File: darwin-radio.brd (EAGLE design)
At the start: 110 x 73 mm, 50 parts, among them J1 S1911-46R, Q2 NDS8434, U1 ATWINC, U2 INA219, U6 MCP7384X

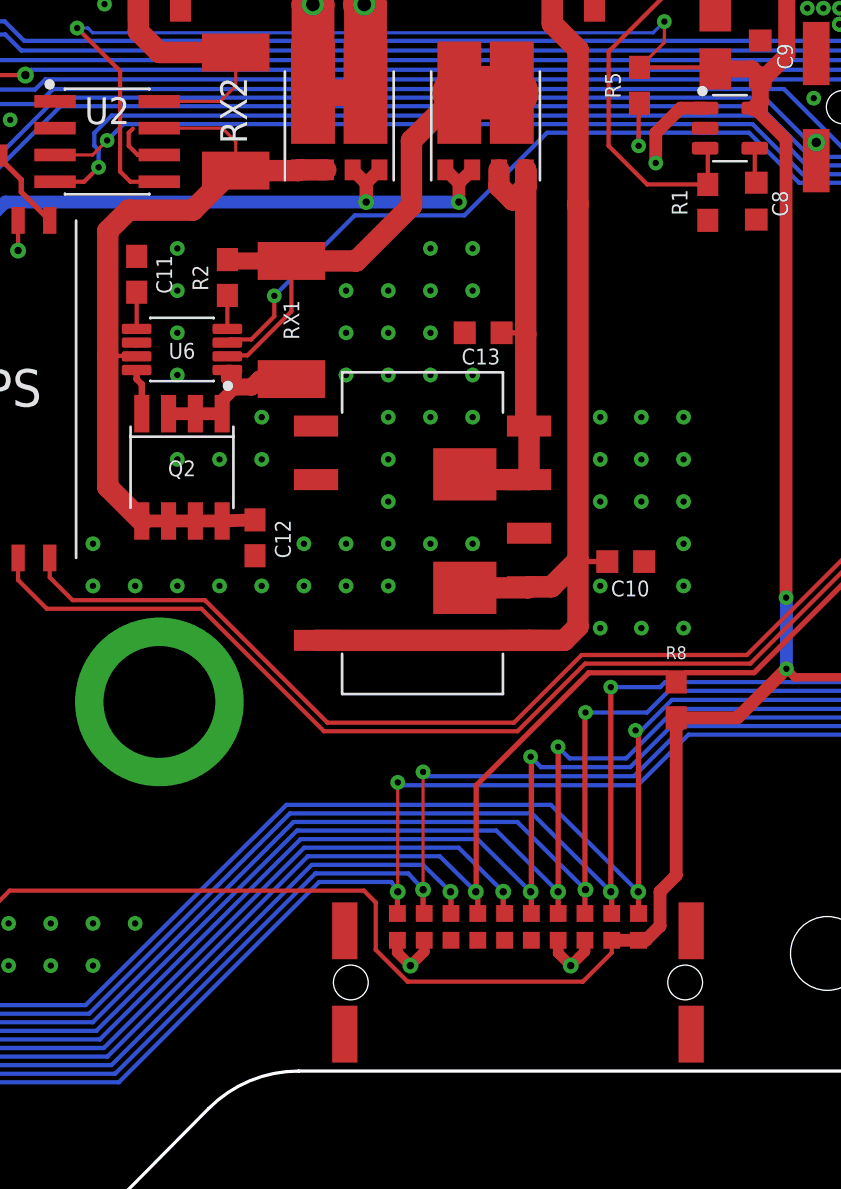
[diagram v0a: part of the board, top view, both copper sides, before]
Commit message: Toughened up connector footprints, cleaned up schematic, added schematic PDF.
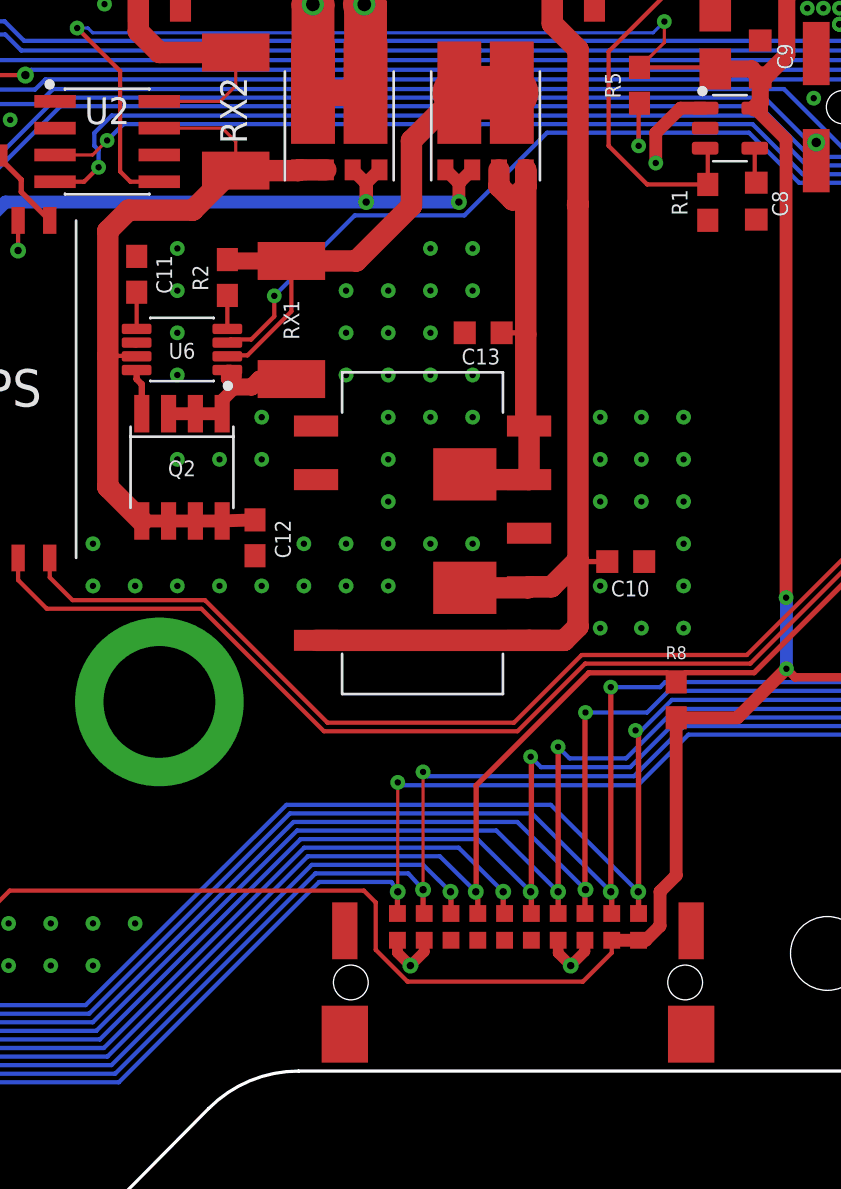
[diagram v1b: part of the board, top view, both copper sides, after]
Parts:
- RX1: value 100M -> 200m
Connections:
- net GND: now also BACKPLANE.PAD0, BACKPLANE.PAD1, BACKPLANE.PAD2, BACKPLANE.PAD3
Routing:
- net GND: track 111.1 -> 108.6 mm

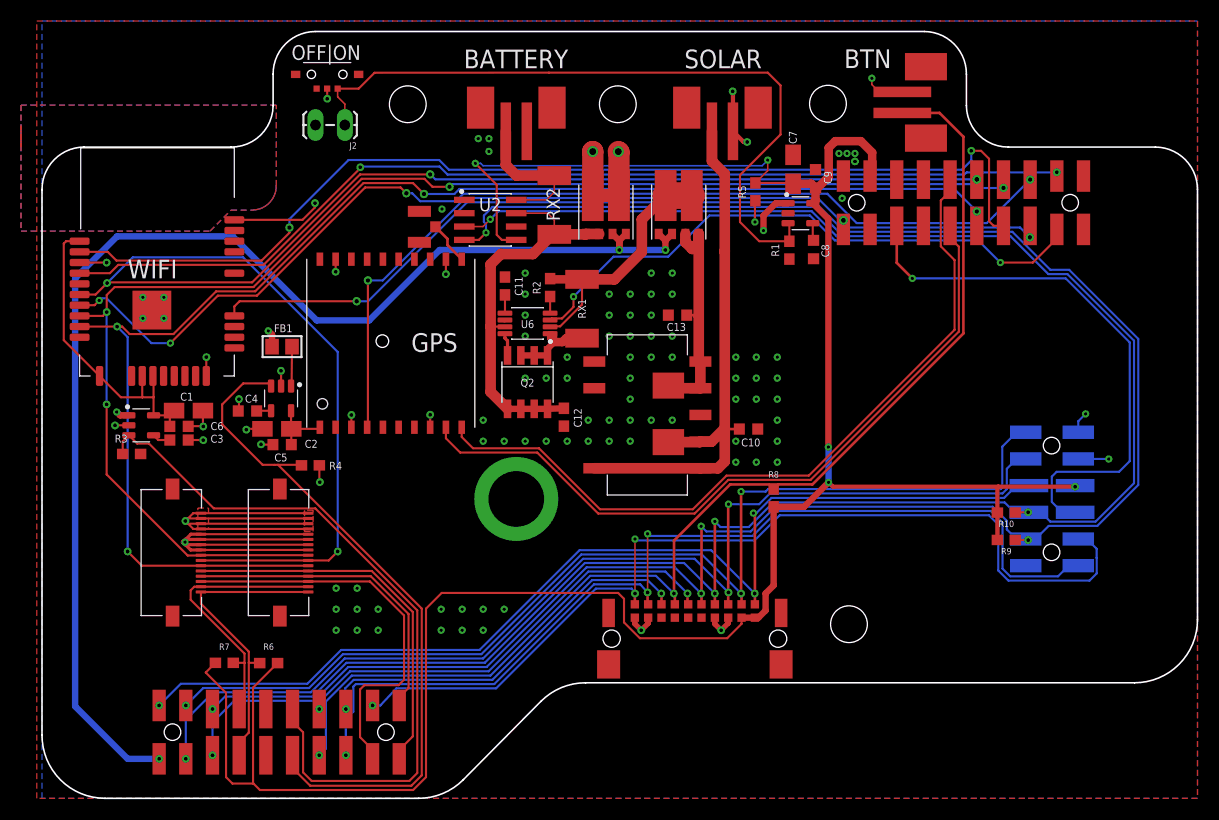
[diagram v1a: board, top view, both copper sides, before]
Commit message: Transitioned from 4 to 2 layers. Added solar power monitor. Changed GPS to L80-M39.
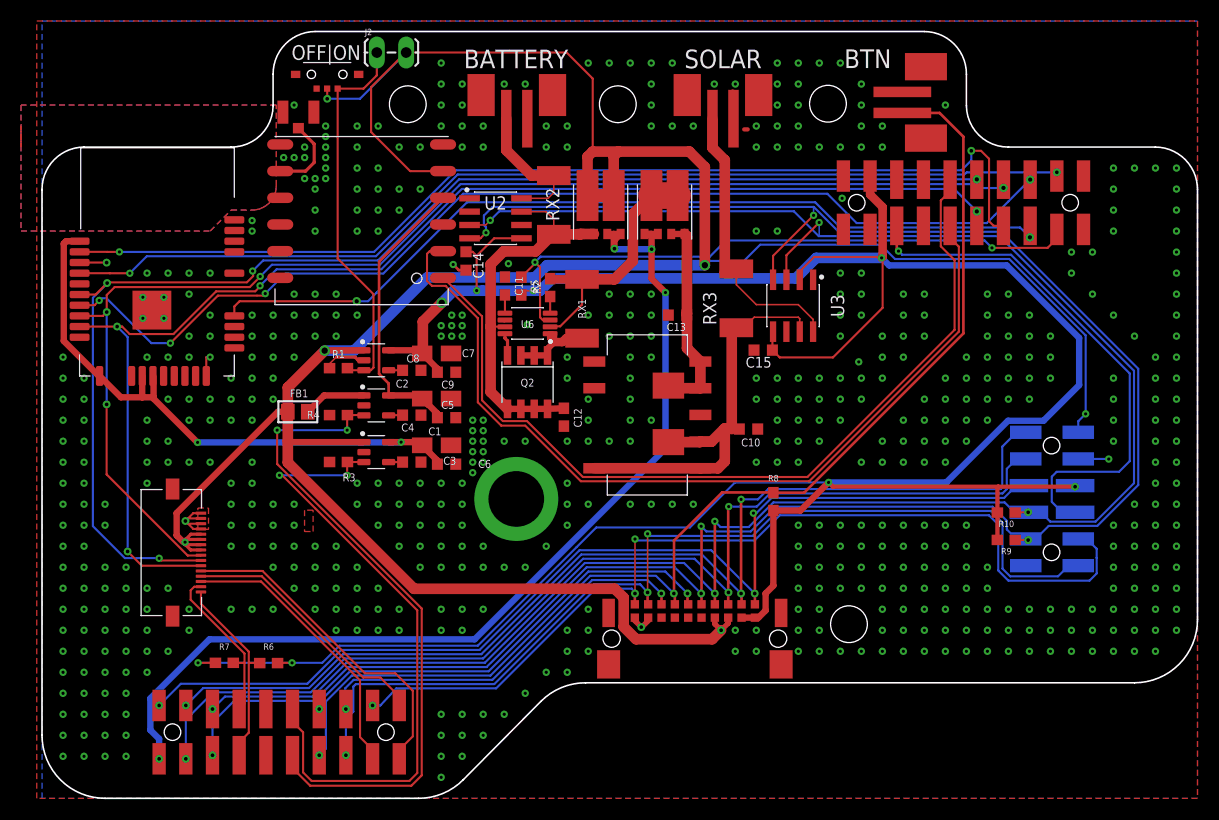
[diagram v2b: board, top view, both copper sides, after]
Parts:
- removed FFC2: 505110-1692, Conservify:505110-1692
- added C14, C15: .1uf, rcl:C0603K
- added RX3: 100M, rcl:R2512
- added U3: INA219, Conservify:SOIC127P599X175-8N
- U$1: value FGPMMOPA6H -> FGPMMOPA6HL80; device Conservify:GPS_MODULE -> Conservify:L80-M39
- moved R1 44.4 mm to (28.2, 41.0), turned to 0 degrees
- moved U$4 42.7 mm to (31.8, 41.7)
- moved C8 39.9 mm to (35.2, 40.7), turned to 0 degrees
- moved C9 39.7 mm to (38.5, 40.6), turned to 0 degrees
- moved C7 38.2 mm to (37.6, 42.3), turned to 180 degrees
- moved C6 25.7 mm to (38.5, 31.8)
- moved R5 24.0 mm to (45.6, 48.8), turned to 90 degrees
- moved C1 23.8 mm to (37.6, 33.6)
- moved U$3 22.5 mm to (31.8, 33.0)
- moved C3 22.3 mm to (35.2, 32.0)
- moved R3 19.7 mm to (28.2, 32.0), turned to 0 degrees
- moved U$11 15.9 mm to (24.4, 65.3), turned to 0 degrees
- moved C5 15.9 mm to (38.5, 36.2), turned to 0 degrees
- moved C4 15.6 mm to (35.2, 36.5), turned to 0 degrees
- moved C2 15.5 mm to (37.6, 38.1), turned to 180 degrees
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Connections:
- new net SOL+RAW: RX3.2, SOLAR-JST.+, U3.8
- net 3V3: now also C14.1, C15.1, U3.2, U3.5
- net GND: now also BAT-JST.PAD1, BAT-JST.PAD2, BTN-JST.PAD1, BTN-JST.PAD2, C14.2, C15.2, SOLAR-JST.PAD1, SOLAR-JST.PAD2, U$1.12, U$1.3, U3.1, U3.6; no longer FFC2.1, FFC2.2, FFC2.3, FFC2.4, U$1.P$12, U$1.P$19, U$1.P$3, U$1.P$8
- net GPS_RX: now also U$1.2; no longer U$1.P$9
- net GPS_TX: now also U$1.1; no longer U$1.P$10
- net MOD_G0: no longer FFC2.13
- net MOD_G13: no longer FFC2.14
- net MOD_G14: no longer FFC2.12
- net MOD_SCL: now also U3.4
- net MOD_SDA: now also U3.3
- net N$3: now also U$1.4; no longer U$1.P$1
- net N$4: now also U$1.11; no longer U$1.P$11
- net RADIO_MISO: no longer FFC2.9
- net RADIO_MOSI: no longer FFC2.10
- net RADIO_SCK: no longer FFC2.11
- net RAD_SCL: no longer FFC2.16
- net RAD_SDA: no longer FFC2.15
- net SOL+: now also RX3.1, U3.7; no longer SOLAR-JST.+
- net UNREG: now also U$1.5; no longer FFC2.5, FFC2.6, FFC2.7, FFC2.8
- net VBACKUP: no longer U$1.P$4
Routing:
- net UNREG: track 73.7 -> 277.8 mm, vias 9 -> 6
- net GND: track 108.6 -> 22.4 mm, vias 105 -> 597
- net VBACKUP: track 63.4 -> 0.00 mm, vias 2 -> 0
- net 3V3: track 230.0 -> 275.4 mm, vias 5 -> 8
- net PSWITCH: track 69.0 -> 37.1 mm
- net SOL+RAW: track 0.00 -> 27.7 mm
- net WIFI_3V3: track 30.6 -> 56.9 mm, vias 0 -> 2
- net V5: track 120.9 -> 95.8 mm, vias 3 -> 4
- net RADIO_MOSI: track 149.4 -> 125.7 mm, vias 5 -> 4
- net N$3: track 6.02 -> 27.5 mm
- net GPS_RX: track 70.4 -> 83.7 mm
- net MOD_G13: track 38.5 -> 27.0 mm
- net SOL+: track 52.0 -> 40.7 mm
- net RAD_SDA: track 26.0 -> 15.8 mm
- net RAD_SCL: track 29.1 -> 18.9 mm
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- removed copper zone on layer 15, net GND
- removed copper zone on layer 2, net UNREG
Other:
- board text removed: "GPS"
- board text removed: "WIFI"
